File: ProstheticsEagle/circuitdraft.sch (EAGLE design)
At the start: 31 parts, among them IC1 BQ25887RGER, IC2 TPS54627DDAR, Q1 16 MHz

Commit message: This is a test
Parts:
- added IC3: AT25P, atmel:AT25P
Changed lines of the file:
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@@
 <part name="AGND16" library="supply1" library_urn="urn:adsk.eagle:library:371" deviceset="AGND" device=""/>
 <part name="BATTERYIO" library="pinhead" library_urn="urn:adsk.eagle:library:325" deviceset="PINHD-1X3" device="" package3d_urn="urn:adsk.eagle:package:22458/2"/>
+<part name="IC3" library="atmel" library_urn="urn:adsk.eagle:library:105" deviceset="AT25*" device="P" package3d_urn="urn:adsk.eagle:package:4324/1"/>
 </parts>
 <sheets>
@@
 <attribute name="VALUE" x="-2.54" y="3.81" size="1.778" layer="96" rot="R90"/>
 </instance>
+<instance part="IC3" gate="G$1" x="7.62" y="152.4" smashed="yes">
+<attribute name="NAME" x="0" y="163.195" size="1.778" layer="95"/>
+<attribute name="VALUE" x="0" y="139.7" size="1.778" layer="96"/>
+</instance>
 </instances>

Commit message: Semi-complete schematic and auto routed board
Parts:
- removed IC3: AT25P, atmel:AT25P
- removed JP1: (no value), pinhead:PINHD-1X4
- removed JP2: (no value), pinhead:PINHD-2X3
- added C13, C17: 1 uF, capacitor-wima:C2,5-3
- added C14: 4.7 uF, capacitor-wima:C2,5-3
- added C15: 47 nF, capacitor-wima:C2,5-3
- added C16: 44 uF, capacitor-wima:C2,5-3
- added C18: 10 uF, capacitor-wima:C2,5-3
- added ISP: (no value), pinhead:PINHD-2X3
- added L2: 1 uH, rcl:L-US0204/7
- added R10, R11, R7, R8, R9: 10000 Ohms, rcl:R-US_0204/7
- added R12: 30.1 kOhms, rcl:R-US_0204/7
- added R13: 5.23 kOhms, rcl:R-US_0204/7
- added R14: 300 Ohms, rcl:R-US_0204/7
- added R6: 12 Ohms, rcl:R-US_0204/7
- added THERMISTOR: (no value), pinhead:PINHD-1X2
- added USB: (no value), pinhead:PINHD-1X4
- R4: value 8250 Ohms -> 124000 Ohms
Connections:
- removed net B-: BATTERYIO.3
- removed net N$16: C11.2, C12.1, L1.2
- new net BTST: C15.2, IC1.BTST
- new net INT: IC1.!INT, R10.1, U$1.(ICP1/ADC8)PD4
- new net N$18: C15.1, IC1.SW_1, L2.2
- new net N$19: C14.1, IC1.REGN, R13.2
- new net N$20: C16.1, IC1.SNS_1
- new net N$21: C18.1, IC1.PMID_1, L2.1
- new net N$3: IC1.CBSET, R6.2
- new net SCL: IC1.SCL, R8.1, U$1.(OSC0B/SCL/INT0)PD0
- new net SDA: IC1.SDA, R7.1, U$1.(SDA/INT1)PD1
- new net STAT: IC1.STAT, R11.1, U$1.(T1/OC4D/ADC9)PD6
- new net TS: IC1.TS, R12.2, R13.1, THERMISTOR.1
- new net VOUT: MYOELECTRIC.1
- net AGND: now also BATTERYIO.3, C13.1, C14.2, C16.2, C17.1, C18.2, IC1.GND_2, IC1.ILIM, ISP.6, R12.1, THERMISTOR.2; no longer JP2.6
- net B+: now also C13.2, C4.2, C5.2, C6.2, IC1.BAT_1, IC2.VIN, R3.1
- net D+: now also USB.2; no longer JP1.2
- net D-: now also USB.3; no longer JP1.3
- net MIDDLE: now also R14.1, R6.1, U$1.(ADC7/TDI)PF7
- net MISO: now also ISP.1; no longer JP2.1
- net MOSI: now also ISP.4; no longer JP2.4
- net N$10: now also IC1.MID, R14.2; no longer C7.2, R4.1
- net N$7: now also IC1.!PG, R9.1; no longer C4.2, C5.2, C6.2, IC2.VIN
- net POWER: now also C11.2, C12.1, C7.2, ISP.2, L1.2, R4.1; no longer JP2.2, MYOELECTRIC.1
- net RST: now also ISP.5; no longer JP2.5
- net SCK: now also ISP.3; no longer JP2.3
- net UGND: now also USB.4; no longer JP1.4
- net VBUS: now also C17.2, IC1.PSEL, IC1.VBUS, R10.2, R11.2, R7.2, R8.2, R9.2, USB.1; no longer JP1.1
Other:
- moved on the sheet: BATTERYIO, C10, C11, C12, C4, C5, C6, C7, C8, C9, IC2, L1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

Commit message: uhh
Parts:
- added LED: (no value), pinhead:PINHD-1X4
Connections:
- new net N$23: LED.4
- new net N$24: LED.1
- net AGND: now also LED.3
- net POWER: now also LED.2
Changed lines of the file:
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@@
 <part name="C18" library="capacitor-wima" library_urn="urn:adsk.eagle:library:116" deviceset="C" device="2,5-3" package3d_urn="urn:adsk.eagle:package:5436/1" value="10 uF"/>
 <part name="AGND24" library="supply1" library_urn="urn:adsk.eagle:library:371" deviceset="AGND" device=""/>
+<part name="LED" library="pinhead" library_urn="urn:adsk.eagle:library:325" deviceset="PINHD-1X4" device="" package3d_urn="urn:adsk.eagle:package:22407/2"/>
 </parts>
 <sheets>
@@
 <instance part="C18" gate="G$1" x="-10.16" y="88.9" smashed="yes" rot="R180"/>
 <instance part="AGND24" gate="VR1" x="17.78" y="-7.62" smashed="yes"/>
+<instance part="LED" gate="A" x="236.22" y="109.22" smashed="yes">
+<attribute name="NAME" x="229.87" y="117.475" size="1.778" layer="95"/>
+<attribute name="VALUE" x="229.87" y="101.6" size="1.778" layer="96"/>
+</instance>
 </instances>
 <busses>
@@
 <wire x1="220.98" y1="27.94" x2="228.6" y2="27.94" width="0.1524" layer="91"/>
 <label x="228.6" y="27.94" size="1.778" layer="95" xref="yes"/>
+</segment>
+<segment>
+<pinref part="LED" gate="A" pin="2"/>
+<wire x1="233.68" y1="111.76" x2="226.06" y2="111.76" width="0.1524" layer="91"/>
+<label x="215.9" y="111.76" size="1.778" layer="95"/>
 </segment>
 </net>
@@
 <wire x1="7.62" y1="-5.08" x2="17.78" y2="-5.08" width="0.1524" layer="91"/>
 <pinref part="AGND24" gate="VR1" pin="AGND"/>
+</segment>
+<segment>
+<pinref part="LED" gate="A" pin="3"/>
+<wire x1="233.68" y1="109.22" x2="226.06" y2="109.22" width="0.1524" layer="91"/>
+<label x="218.44" y="109.22" size="1.778" layer="95"/>
 </segment>
 </net>
@@
 </segment>
 </net>
+<net name="N$23" class="0">
+<segment>
+<pinref part="LED" gate="A" pin="4"/>
+<wire x1="233.68" y1="106.68" x2="226.06" y2="106.68" width="0.1524" layer="91"/>
+</segment>
+</net>
+<net name="N$24" class="0">
+<segment>
+<pinref part="LED" gate="A" pin="1"/>
+<wire x1="233.68" y1="114.3" x2="226.06" y2="114.3" width="0.1524" layer="91"/>
+</segment>
+</net>

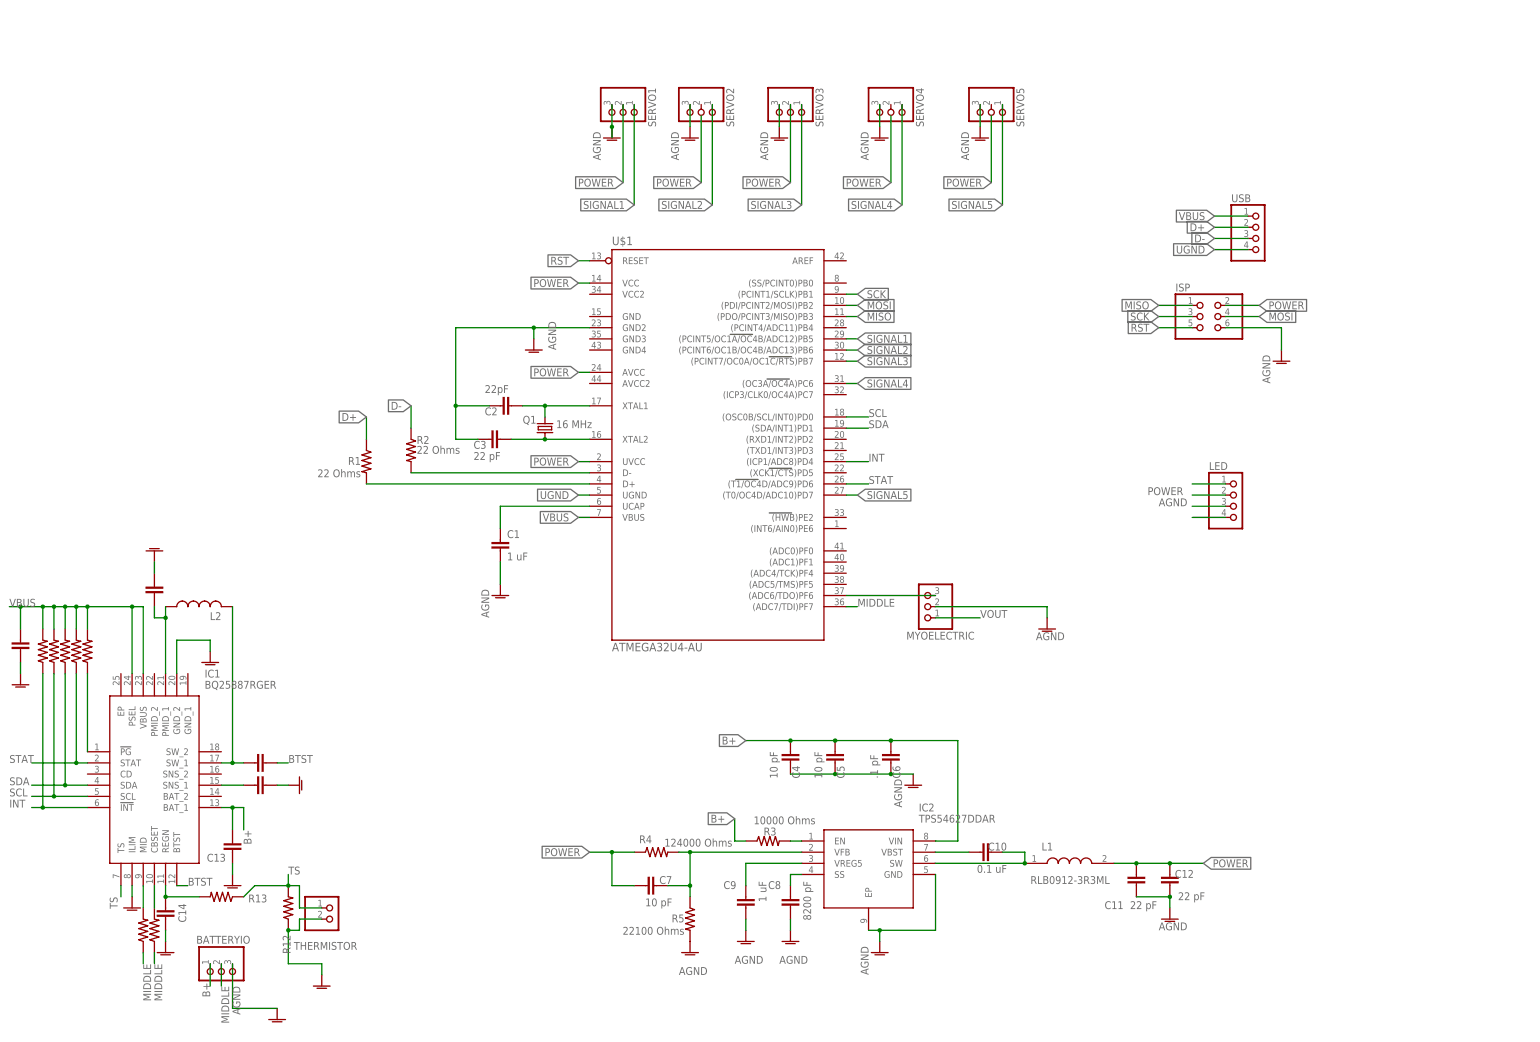
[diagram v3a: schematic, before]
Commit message: Added surface mount parts
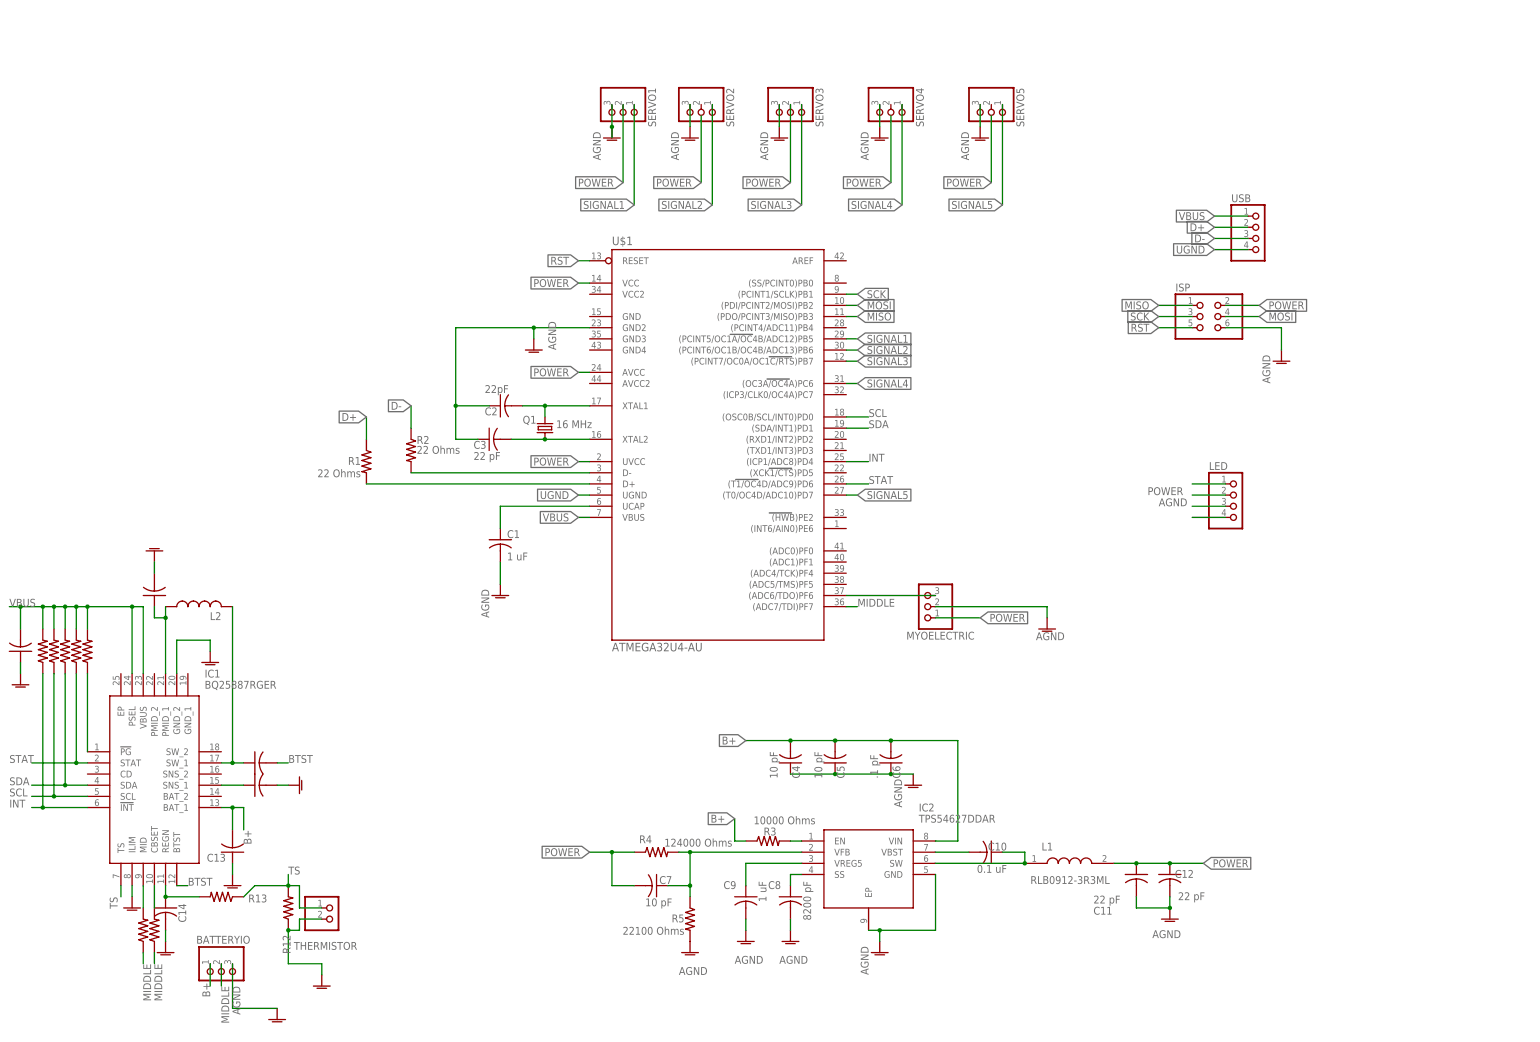
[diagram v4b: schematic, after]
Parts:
- C1, C10, C11, C12, C13, C14, C15, C16, C17, C18, C2, C3, C4, C5, C6, C7, C8, C9: device capacitor-wima:C2,5-3 -> rcl:C-USC0805
- R1, R10, R11, R12, R13, R14, R2, R3, R4, R5, R6, R7, R8, R9: device rcl:R-US_0204/7 -> rcl:R-US_R0603
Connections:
- removed net N$17: C11.1, C12.2
- removed net VOUT: MYOELECTRIC.1
- net AGND: now also C11.2, C12.2
- net POWER: now also C11.1, MYOELECTRIC.1; no longer C11.2
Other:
- moved on the sheet: C11

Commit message: fffff
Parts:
- removed MYOELECTRIC: (no value), pinhead:PINHD-1X3
- added MYO: (no value), pinhead:PINHD-1X3
- LED: device pinhead:PINHD-1X4 -> pinhead:PINHD-1X3
- renumbered BATTERYIO to BATIO, THERMISTOR to TS
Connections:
- removed net N$12: MYOELECTRIC.3, U$1.(ADC6/TDO)PF6
- removed net N$23: LED.4
- removed net N$24: LED.1
- new net DATAIN: LED.3
- new net MYOSIGNAL: MYO.3, U$1.(ADC6/TDO)PF6
- net AGND: now also LED.2, MYO.2; no longer LED.3, MYOELECTRIC.2
- net POWER: now also LED.1, MYO.1, SERVO2.2, SERVO4.2, SERVO5.2; no longer LED.2, MYOELECTRIC.1

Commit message: moved stuff
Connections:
- net DATAIN: now also U$1.(ICP3/CLK0/OC4A)PC7
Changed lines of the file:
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@@
 <label x="205.74" y="91.44" size="1.778" layer="95"/>
+</segment>
+<segment>
+<pinref part="U$1" gate="G$1" pin="(ICP3/CLK0/OC4A)PC7"/>
+<wire x1="147.32" y1="134.62" x2="149.86" y2="134.62" width="0.1524" layer="91"/>
+<label x="149.86" y="132.08" size="1.778" layer="95"/>
 </segment>
 </net>

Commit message: Ahmad's revision
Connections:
- net DATAIN: now also U$1.(PCINT7/OC0A/OC1C/RTS)PB7; no longer U$1.(ICP3/CLK0/OC4A)PC7
- net MYOSIGNAL: now also U$1.(ADC0)PF0; no longer U$1.(ADC6/TDO)PF6
- net SIGNAL3: now also U$1.(ICP3/CLK0/OC4A)PC7; no longer U$1.(PCINT7/OC0A/OC1C/RTS)PB7
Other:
- moved on the sheet: BATIO, C1, C10, C11, C12, C13, C14, C2, C3, C4, C5, C6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
